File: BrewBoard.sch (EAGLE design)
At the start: 21 parts, among them J1 BATT, J2 AUX, J3 SPK, J5 PIXEL, J6 STAR, J7 MAIN, J8 String, Q1 2n7002k, Q2 2n7002k, Q3 2n7002k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

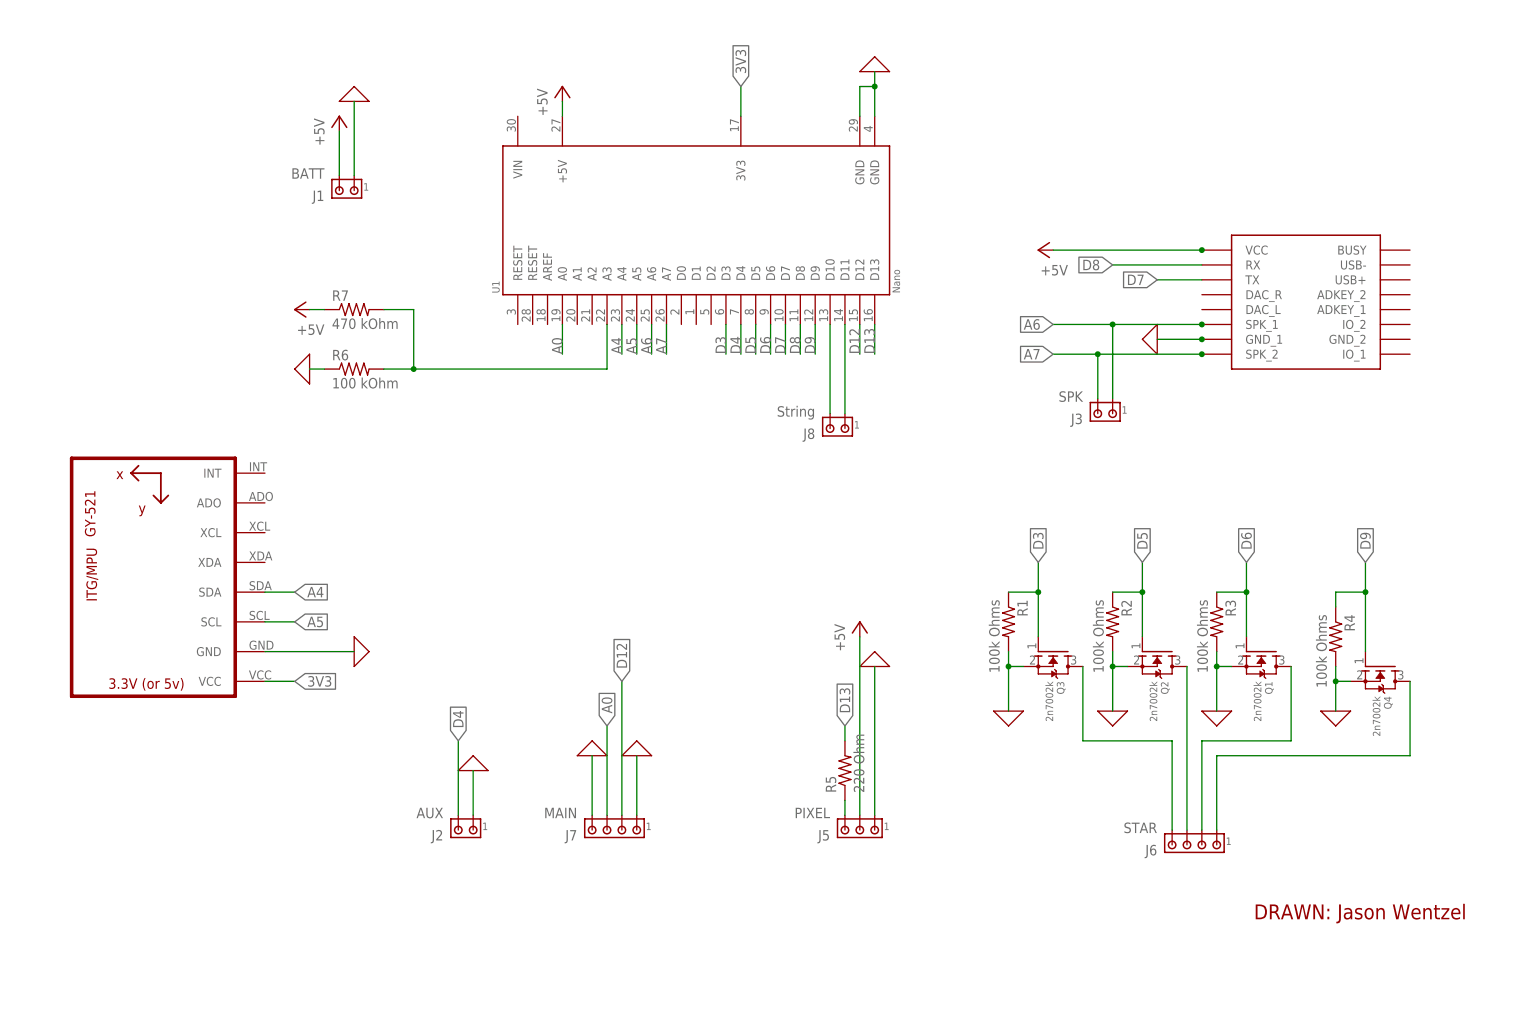
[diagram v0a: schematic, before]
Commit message: Brewboard V3 Update
Adding New Version 3 Update of Brewboard
Feature/Change List;
- Interrupt mode is now available for clashes.
- All extra Pins have pads (for folks that want to experiment and add features).
- LED Power Traces are now able to handle a total of 7.8A so Pixel Blades can be safely hooked up to MOSFETs (less drain in deepsleep).
- Power Traces for Pixels removed! Pixel Blade can be wired directly from the battery Positive, and to two or three of the RGB MOSFET pads as mentioned above.
- 4th MOSFET removed to reduce part count.
- Pixel Data Line resistor removed, as it really should be on the blade side (also reduces part count).
- All Pins are now Labelled and should now be large enough to be readable.
- Added a few Vias for better overall grounds.
- Spiffy new logo!
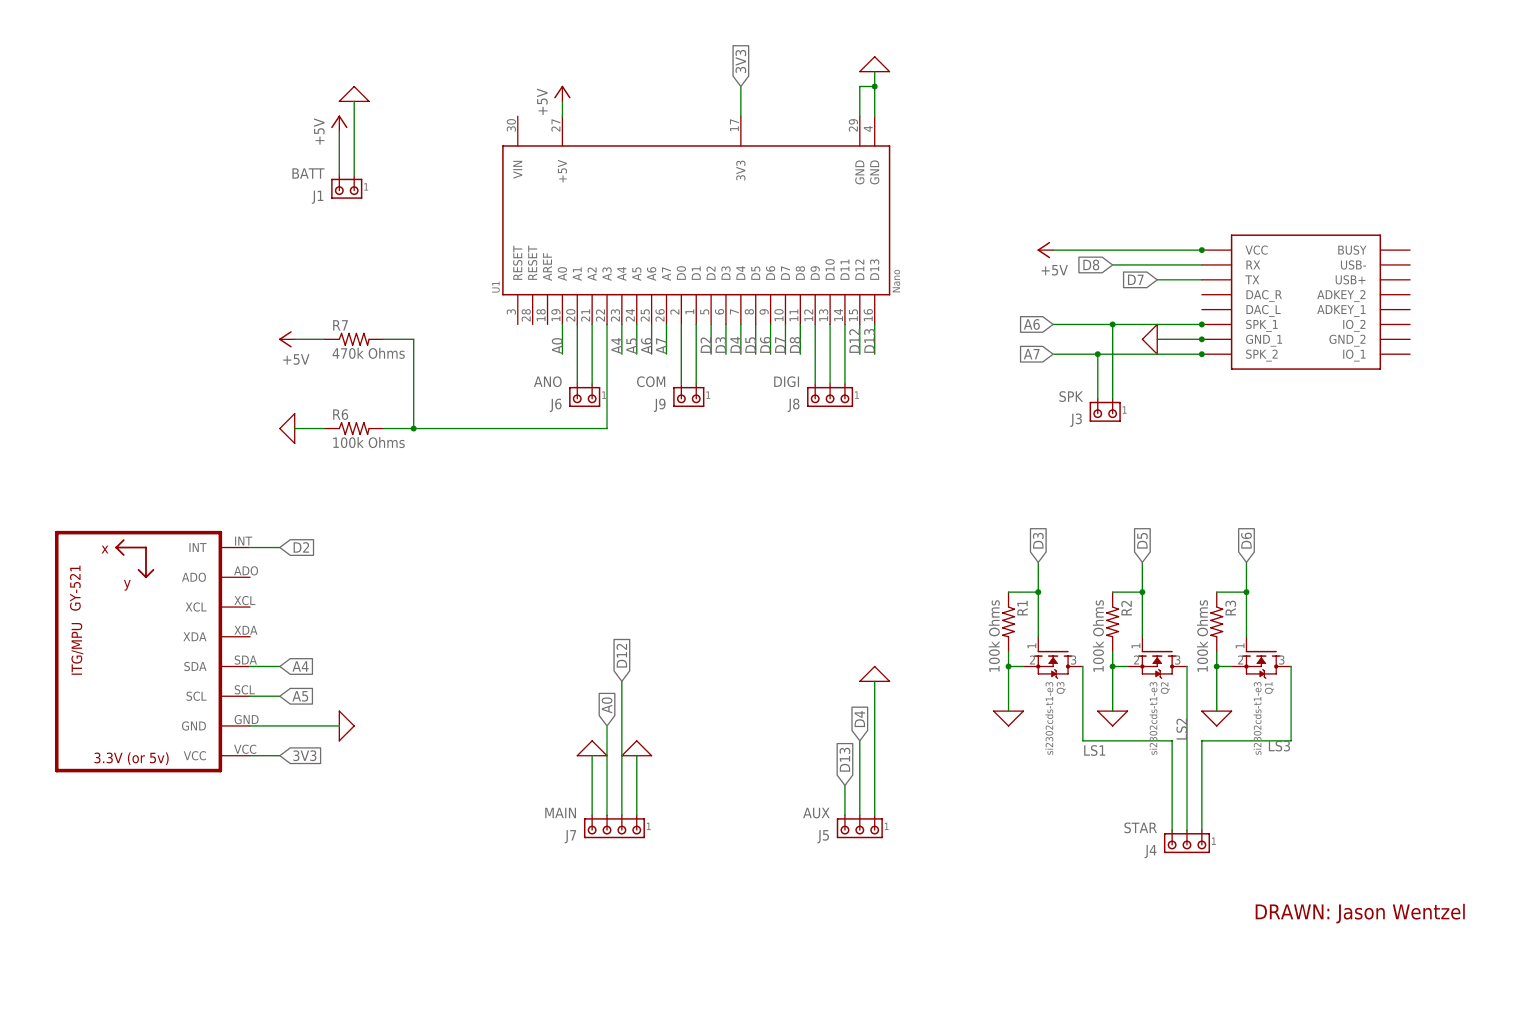
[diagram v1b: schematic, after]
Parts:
- removed J2: AUX, BrewBoard:MTA02-100
- removed Q4: 2n7002k, BrewBoard:MOSFET-NREFLOW
- removed R4: 100k Ohms, BrewBoard:R-US_R0805
- removed R5: 220 Ohm, BrewBoard:R-US_R0805
- added J4: STAR, BrewBoard:MTA03-100
- added J9: COM, BrewBoard:MTA02-100
- J5: value PIXEL -> AUX
- J6: value STAR -> ANO; device BrewBoard:MTA04-100 -> BrewBoard:MTA02-100
- J8: value String -> DIGI; device BrewBoard:MTA02-100 -> BrewBoard:MTA03-100
- Q1, Q2, Q3: value 2n7002k -> si2302cds-t1-e3
- R6: value 100 kOhm -> 100k Ohms
- R7: value 470 kOhm -> 470k Ohms
- renumbered U$1 to U3
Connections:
- net N$16 renamed D11
- net N$7 renamed D10
- removed net N$23: J6.2, Q1.D
- removed net N$24: J6.3, Q2.D
- removed net N$25: J6.4, Q3.D
- removed net N$28: J6.1, Q4.D
- removed net N$9: J5.3, R5.1
- new net A1: J6.2, U1.A1
- new net A2: J6.1, U1.A2
- new net D2: U1.D2, U2.INT
- new net LS1: J4.3, Q3.D
- new net LS2: J4.2, Q2.D
- new net LS3: J4.1, Q1.D
- new net N$1: J9.2, U1.D0
- new net N$2: J9.1, U1.D1
- net +5V: no longer J5.2
- net 0: no longer J2.1, Q4.S, R4.2
- net D13: now also J5.3; no longer R5.2
- net D4: now also J5.2; no longer J2.2
- net D9: now also J8.3; no longer Q4.G, R4.1
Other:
- moved on the sheet: R6, R7

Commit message: Updated to V4
Updated source files to V4 and deleted PDF version of Schematic
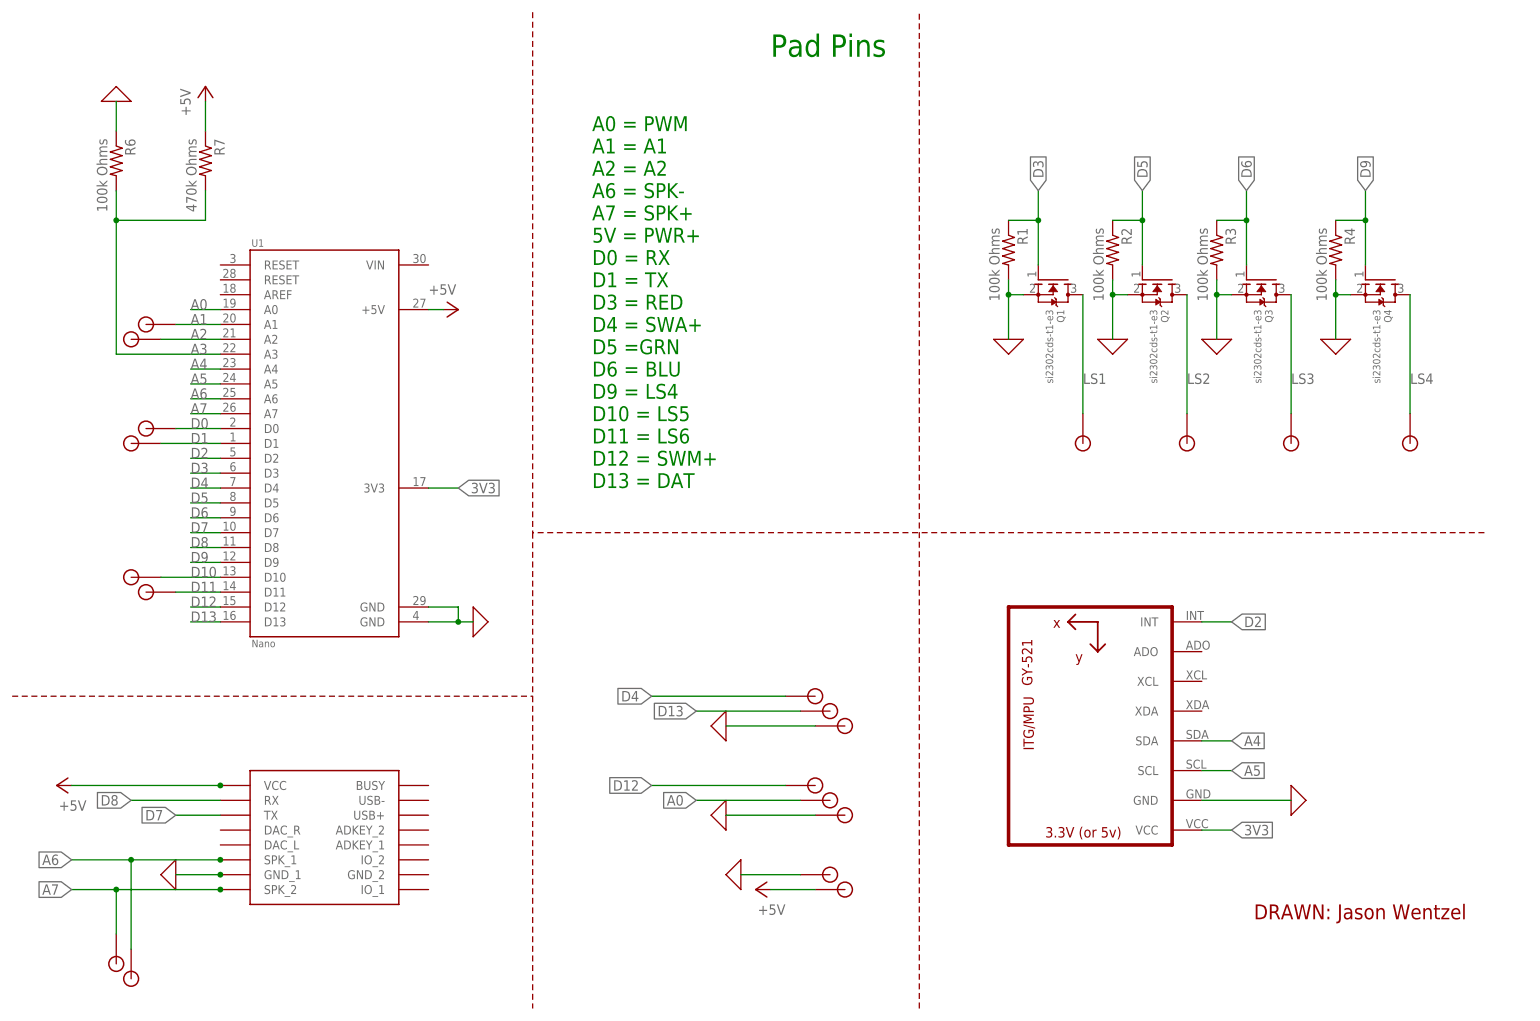
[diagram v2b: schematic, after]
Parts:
- removed J1: BATT, BrewBoard:MTA02-100
- removed J3: SPK, BrewBoard:MTA02-100
- removed J4: STAR, BrewBoard:MTA03-100
- removed J5: AUX, BrewBoard:MTA03-100
- removed J6: ANO, BrewBoard:MTA02-100
- removed J7: MAIN, BrewBoard:MTA04-100
- removed J8: DIGI, BrewBoard:MTA03-100
- removed J9: COM, BrewBoard:MTA02-100
- added LS1, SPK+, U$1, U$11, U$12, U$13, U$15, U$16, U$17, U$18, U$19, U$22, U$27, U$28, U$4, U$5, U$6, U$7, U$8, U$9: SINGLE_ONE_SIDE_PAD, BrewboardV4:SINGLE_ONE_SIDE_PAD
- added Q4: si2302cds-t1-e3, BrewBoard:MOSFET-NREFLOW
- added R4: 100k Ohms, BrewBoard:R-US_R0805
- U1: device BrewBoard:A000005SIMPLE -> BrewBoard:A000005NANO_SLIM
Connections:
- net N$14 renamed A3
- removed net N$1: J9.2, U1.D0
- removed net N$2: J9.1, U1.D1
- new net D0: U$5.P$1, U1.D0
- new net D1: U$6.P$1, U1.D1
- new net LS4: Q4.D, U$7.P$1
- net +5V: now also U$12.P$1; no longer J1.2
- net 0: now also Q4.S, R4.2, U$13.P$1, U$17.P$1, U$27.P$1; no longer J1.1, J5.1, J7.1, J7.4
- net A0: now also U$18.P$1; no longer J7.3
- net A1: now also U$1.P$1; no longer J6.2
- net A2: now also U$4.P$1; no longer J6.1
- net A6: now also U$11.P$1; no longer J3.1
- net A7: now also SPK+.P$1; no longer J3.2
- net D10: now also U$8.P$1; no longer J8.2
- net D11: now also U$9.P$1; no longer J8.1
- net D12: now also U$19.P$1; no longer J7.2
- net D13: now also U$28.P$1; no longer J5.3
- net D3: now also Q1.G; no longer Q3.G
- net D4: now also U$22.P$1; no longer J5.2
- net D6: now also Q3.G; no longer Q1.G
- net D9: now also Q4.G, R4.1; no longer J8.3
- net LS1: now also LS1.P$1, Q1.D; no longer J4.3, Q3.D
- net LS2: now also U$15.P$1; no longer J4.2
- net LS3: now also Q3.D, U$16.P$1; no longer J4.1, Q1.D
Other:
- note added: "A0 = PWM A1 = A1 A2 = A2 A6 = SPK- A7 = SPK+ 5V = PWR+ D0 = RX D1 = TX D3 = RED D4 = SWA+ D5 =GRN D6 = BLU D9 = LS4 D10 = LS5 D11 = LS6 D12 = SWM+ D13 = DAT"
- note added: "DFPlayer"
- note added: "MOSFETs"
- note added: "MPU6050"
- note added: "Nano"
- note added: "Pad Pins"
- note added: "Pads"
- moved on the sheet: Q1, Q2, Q3, R1, R2, R3, R6, R7, U1
